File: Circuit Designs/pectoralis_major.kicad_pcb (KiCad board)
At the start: 4 copper layers, 100 x 100 mm, 293 parts, among them J1 0524651671, J2 0533071071, J3 0533071071, J4 0524651071, J5 SoicBite, Q1 AO3400A, Q2 AO3400A, Q3 BUK7V4R2, Q4 BUK7V4R2, Q5 BUK7V4R2, T1 B3380, T2 B3380, U1 TCAN330, U10 INA199A1, U11 AS5047P, U2 STM32F405RGTx, U3 AP2127, U4 AP2127, U5 AP2127, U6 AP2127, U7 DRV8301, U8 INA199A1, U9 INA199A1, Y1 CSTNE8M00

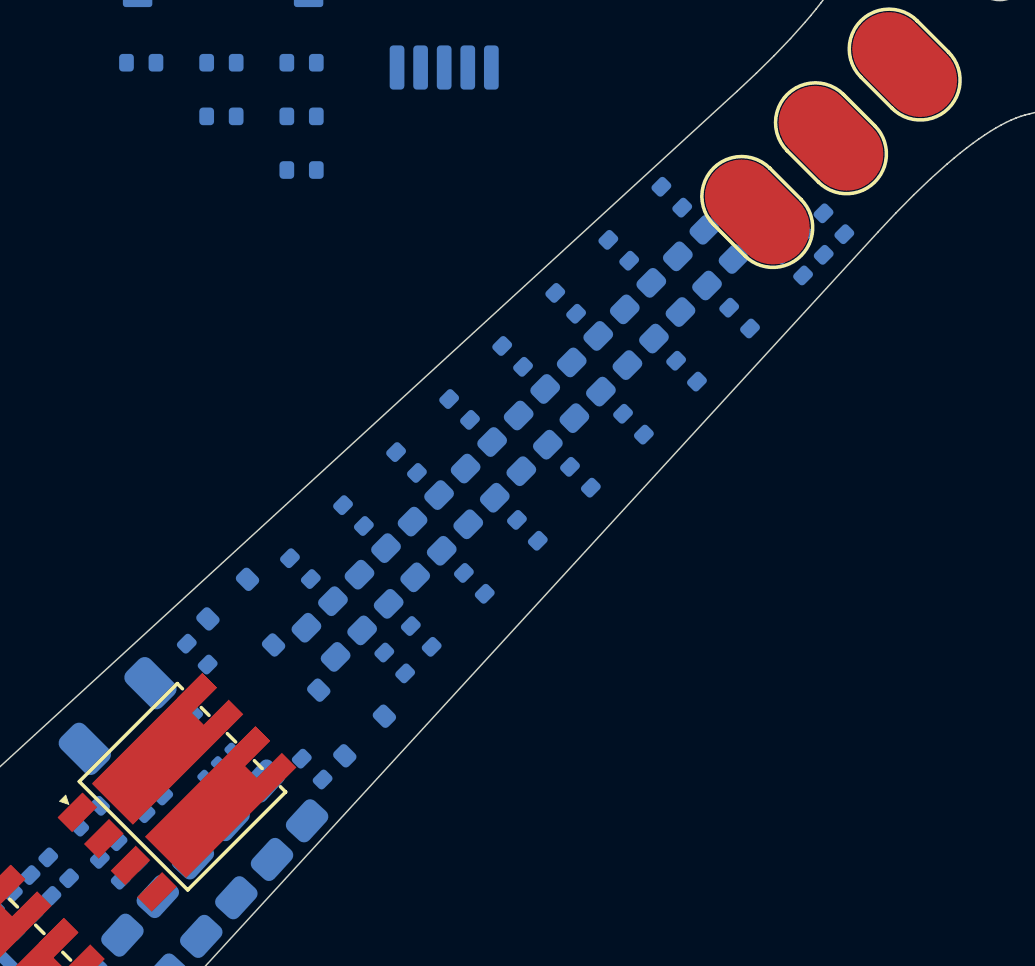
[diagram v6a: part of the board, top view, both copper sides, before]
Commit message: drew the traces in the light section
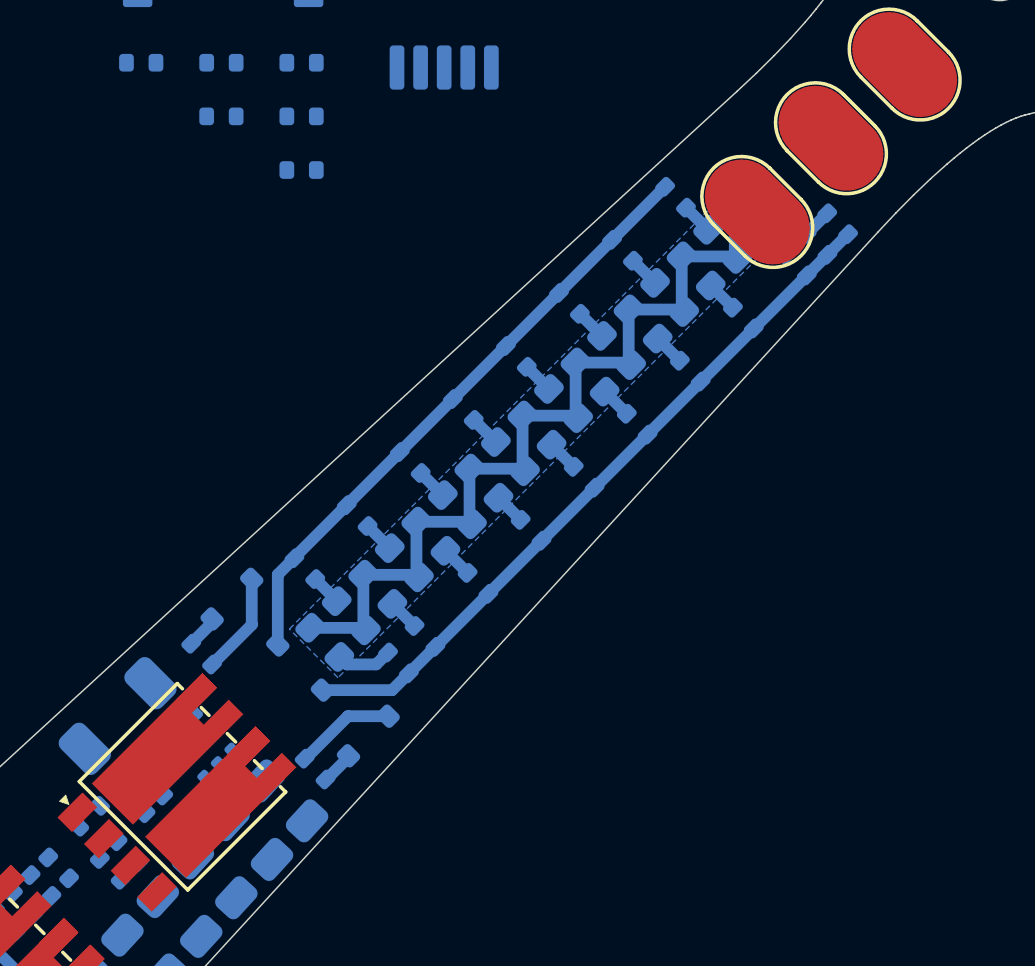
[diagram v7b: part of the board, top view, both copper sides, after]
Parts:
- moved R30 0.15 mm to (151.2, 95.6)
- moved R35 0.15 mm to (147.7, 98.5)
- moved Q2 0.14 mm to (149.5, 97.4)
- moved D1 0.13 mm to (166.2, 83.7)
- moved D10 0.13 mm to (158.1, 91.8)
- moved D11 0.13 mm to (157.2, 92.7)
- moved D12 0.13 mm to (156.3, 93.6)
- moved D14 0.13 mm to (154.5, 95.4)
- moved D15 0.13 mm to (153.6, 96.3)
- moved D16 0.13 mm to (152.7, 97.2)
- moved D17 0.13 mm to (151.8, 98.1)
- moved D2 0.13 mm to (165.3, 84.6)
- moved D4 0.13 mm to (163.5, 86.4)
- moved D5 0.13 mm to (162.6, 87.3)
- moved D6 0.13 mm to (161.7, 88.2)
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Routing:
- net +3V3: track 0.00 -> 29.8 mm
- net Net-(Q1-Pad3): track 0.00 -> 24.2 mm
- net Net-(Q2-Pad3): track 0.00 -> 21.0 mm
- net GND: track 0.00 -> 5.56 mm
- net /uController/LED_AMBER: track 0.00 -> 3.40 mm
- net Net-(D17-Pad1): track 0.00 -> 1.92 mm
- net /uController/LED_RED: track 0.00 -> 1.14 mm
- net Net-(D8-Pad1): track 0.00 -> 1.06 mm
- net Net-(D5-Pad1): track 0.00 -> 1.06 mm
- net Net-(D3-Pad1): track 0.00 -> 1.06 mm
- net Net-(D15-Pad1): track 0.00 -> 1.06 mm
- net Net-(D13-Pad1): track 0.00 -> 1.06 mm
- net Net-(D10-Pad1): track 0.00 -> 1.06 mm
- net Net-(D9-Pad1): track 0.00 -> 1.06 mm
- net Net-(D7-Pad1): track 0.00 -> 1.06 mm
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- added copper zone on B.Cu, net +3V3

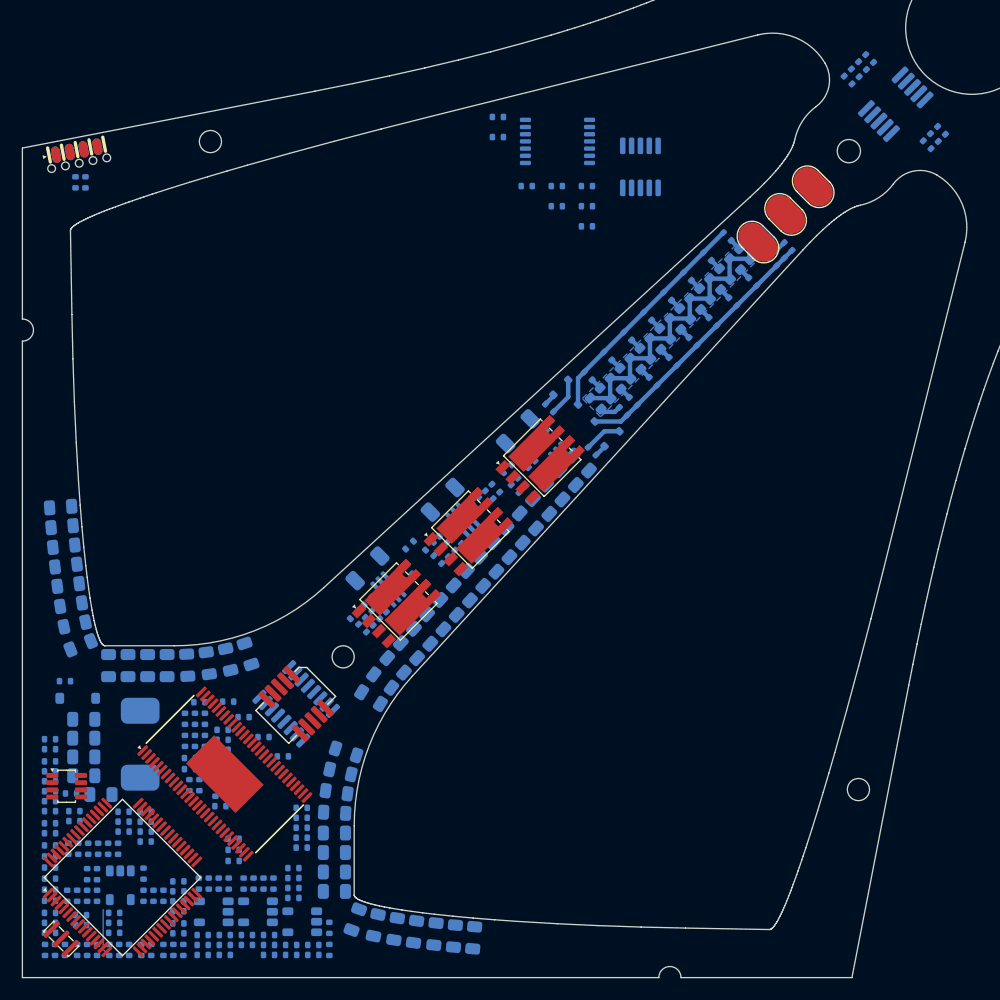
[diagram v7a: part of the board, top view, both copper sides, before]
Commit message: done placing and routing of the golgi tendon organ
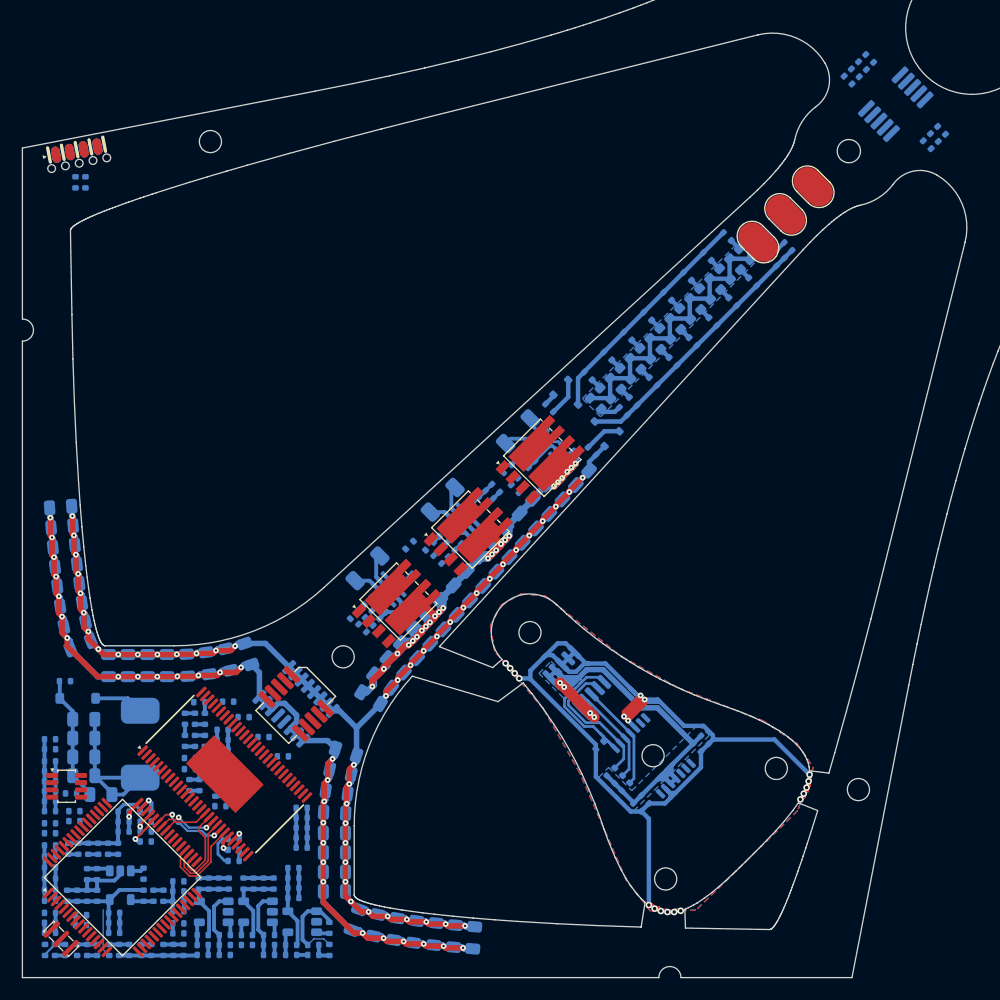
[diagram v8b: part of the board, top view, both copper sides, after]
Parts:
- moved C154 61.4 mm to (156.3, 133.9), turned to -45 degrees
- moved R88 60.9 mm to (153.9, 132.1), turned to 45 degrees
- moved C157 57.0 mm to (155.6, 134.6), turned to -45 degrees
- moved U11 56.2 mm to (157.0, 129.9), turned to -45 degrees
- moved R89 53.0 mm to (153.2, 131.4), turned to 45 degrees
- moved R87 52.6 mm to (154.5, 132.8), turned to 45 degrees
- moved R90 50.7 mm to (152.2, 129.0), turned to -135 degrees
- moved C155 50.1 mm to (161.7, 128.5), turned to -45 degrees
- moved C156 48.2 mm to (161.0, 129.2), turned to -45 degrees
- moved J4 46.7 mm to (150.1, 123.0), turned to -135 degrees
- turned J3 to 135 degrees
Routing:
- net GND: track 5.56 -> 281.5 mm, vias 0 -> 45
- net PVDD2: track 0.00 -> 216.6 mm, vias 0 -> 51
- net /Proprioception/ENC_GND: track 0.00 -> 108.6 mm, vias 0 -> 19
- net /Proprioception/ENC_PWR: track 0.00 -> 58.8 mm, vias 0 -> 4
- net +5VA: track 0.00 -> 32.0 mm
- net +5V: track 0.00 -> 29.1 mm
- net +3V3: track 29.8 -> 54.4 mm, vias 0 -> 1
- net /Proprioception/ENC_nCS: track 0.00 -> 13.6 mm
- net /Proprioception/ENC_SCK: track 0.00 -> 12.7 mm
- net +2V5: track 0.00 -> 11.9 mm
- net +3.3VA: track 0.00 -> 10.4 mm
- net /Proprioception/ENC_MOSI: track 0.00 -> 9.75 mm
- net /Proprioception/ENC_MISO: track 0.00 -> 8.79 mm
- net /powerDrivers/INL_C: track 0.00 -> 8.49 mm
- net /powerDrivers/INL_B: track 0.00 -> 7.78 mm
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- added copper zone on B.Cu, net /Proprioception/ENC_GND
- added copper zone on F.Cu, net /Proprioception/ENC_GND
- added copper zone on B.Cu, net /Proprioception/ENC_PWR
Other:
- outline, holes or cut-outs redrawn
